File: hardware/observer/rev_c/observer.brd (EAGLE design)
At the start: 49.5 x 60.2 mm, 61 parts, among them J1 CON_HEADER_2X05-SMD+SHROUDED, J2 CON_HEADER_2X05-SMD+SHROUDED, J3 TC2030-CC2538-BL-NL, J4 JUMPER-PTH-2-NO, J5 PINHD-2X8/SMD, J6 CON_HEADER_2X05-PTH+SHROUDED_A, P9/P8 BBB_HEADER, U1 LPS331AP, U10 TPS62740, U11 DMG1013UW-7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

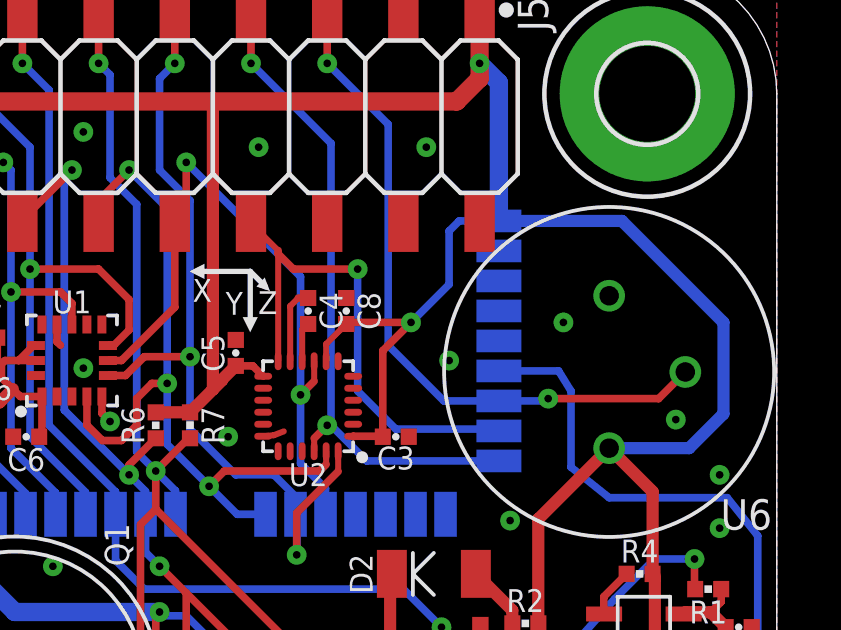
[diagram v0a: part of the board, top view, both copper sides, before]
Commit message: connected opamp gate signal to header for debugging
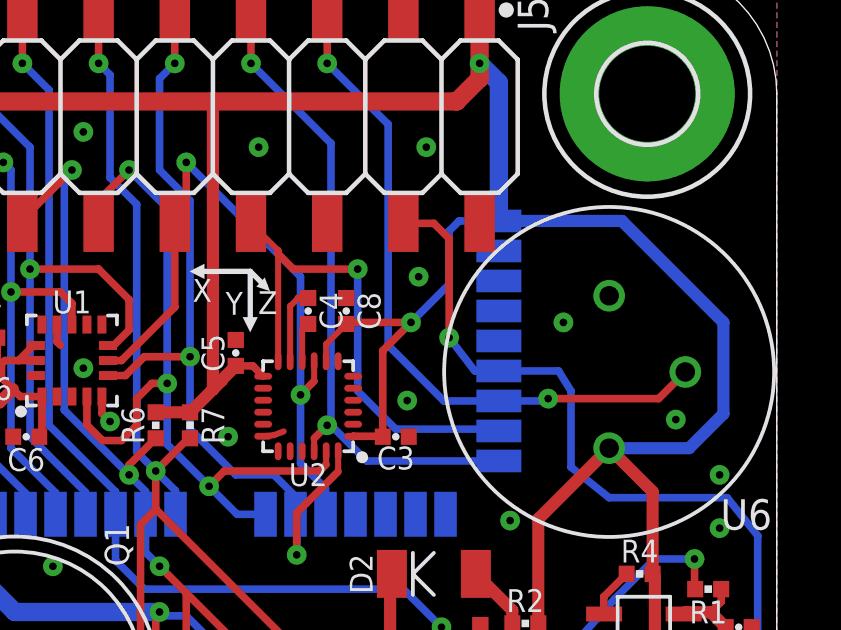
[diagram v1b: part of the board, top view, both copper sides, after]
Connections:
- removed net N$20: J5.4
- net OPAMP_GATE: now also J5.4
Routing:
- net OPAMP_GATE: track 23.3 -> 30.5 mm, vias 1 -> 2
- net GND: vias 40 -> 41
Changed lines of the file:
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@@
 <contactref element="J5" pad="2"/>
 <via x="42.418" y="29.972" extent="1-16" drill="0.254"/>
-<via x="38.608" y="28.702" extent="1-16" drill="0.254"/>
+<via x="37.211" y="27.3685" extent="1-16" drill="0.254"/>
 <via x="31.242" y="26.162" extent="1-16" drill="0.254"/>
 <wire x1="33.309" y1="28.678" x2="33.309" y2="30.515" width="0.2032" layer="1"/>
@@
 <wire x1="6.858" y1="15.875" x2="9.652" y2="15.875" width="0.2032" layer="1"/>
 <wire x1="6.7945" y1="19.431" x2="9.4615" y2="19.431" width="0.2032" layer="16"/>
+<via x="37.592" y="31.496" extent="1-16" drill="0.254"/>
 </signal>
 <signal name="N$3">
@@
 <contactref element="J5" pad="3"/>
 </signal>
-<signal name="N$20">
-<contactref element="J5" pad="4"/>
-</signal>
 <signal name="UNUSED3">
 <contactref element="J5" pad="6"/>
@@
 <via x="48.514" y="13.462" extent="1-16" drill="0.254"/>
 <wire x1="48.514" y1="13.462" x2="48.895" y2="13.97" width="0.254" layer="16"/>
+<contactref element="J5" pad="4"/>
+<wire x1="37.084" y1="33.274" x2="38.1" y2="33.274" width="0.254" layer="1"/>
+<wire x1="38.1" y1="33.274" x2="38.608" y2="32.766" width="0.254" layer="1"/>
+<wire x1="38.608" y1="32.766" x2="38.608" y2="29.464" width="0.254" layer="1"/>
+<via x="38.608" y="29.464" extent="1-16" drill="0.254"/>
+<wire x1="38.608" y1="29.464" x2="39.4631" y2="28.3549" width="0.254" layer="16"/>
+<wire x1="39.4631" y1="28.3549" x2="40.2669" y2="28.3549" width="0.254" layer="16"/>
 </signal>
 </signals>
